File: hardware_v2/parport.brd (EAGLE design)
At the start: 65 x 56 mm, 5 parts, among them K1 PIN20X2, U1 SN74LVC161284DL

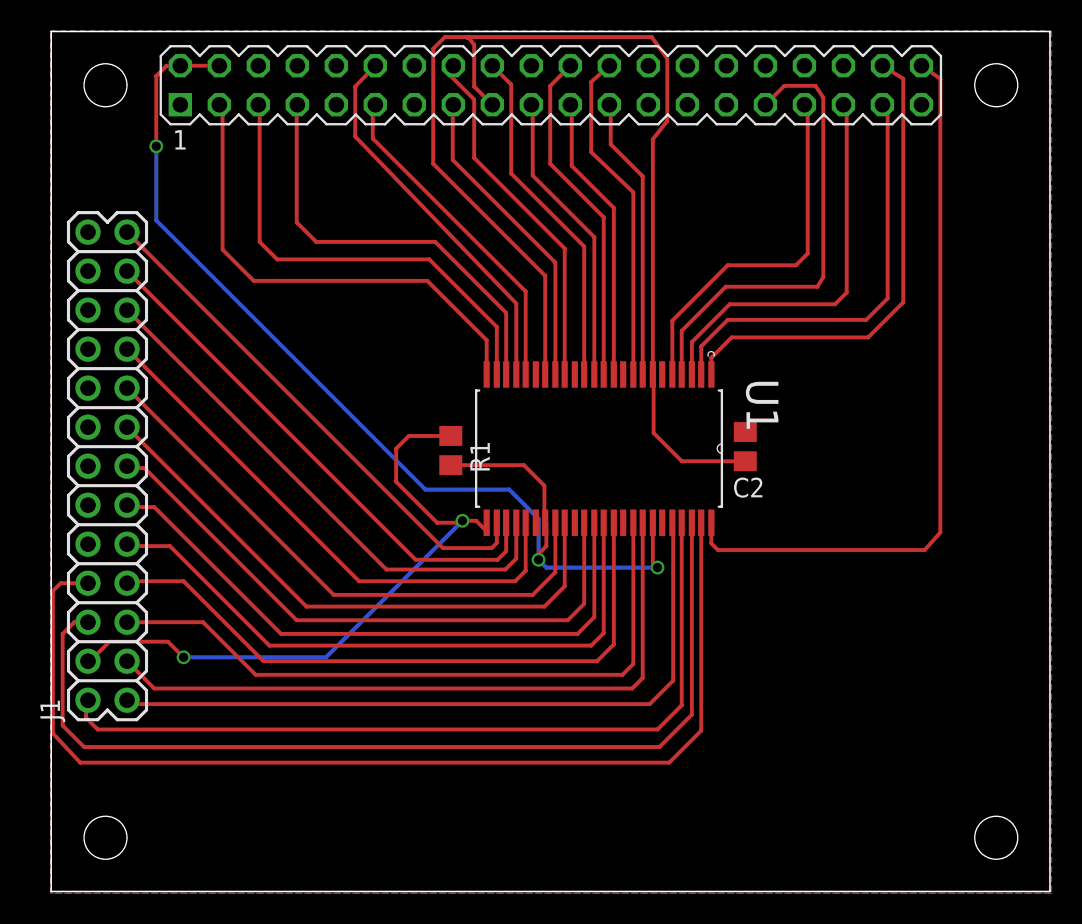
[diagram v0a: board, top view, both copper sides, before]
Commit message: hardware_v2: fix drc errors, add silk title
This version ordered from OSH Park (3 boards).
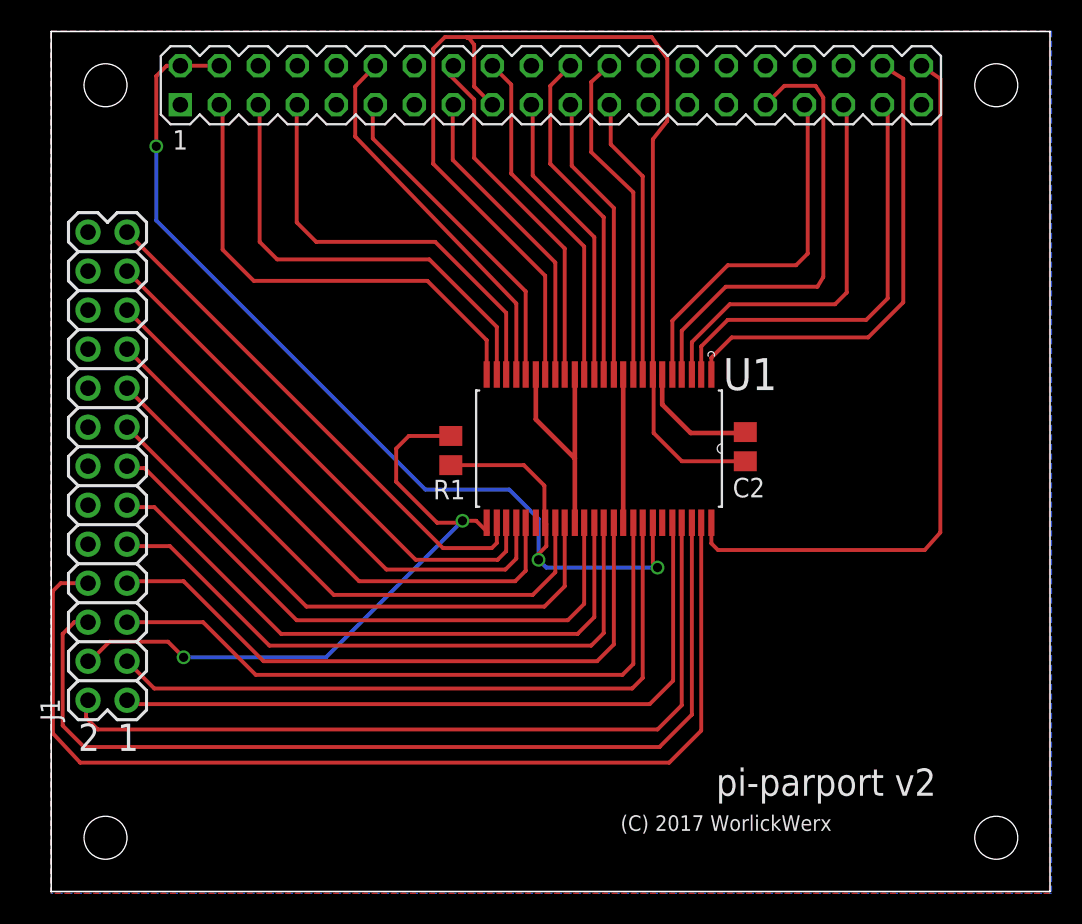
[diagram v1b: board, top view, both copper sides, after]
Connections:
- net GND: now also U1.19, U1.6
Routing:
- net GND: track 0.00 -> 34.0 mm
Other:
- board text added: "(C) 2017 WorlickWerx"
- board text added: "1"
- board text added: "2"
- board text added: "pi-parport v2"
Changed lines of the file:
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@@
 <wire x1="110.9" y1="59.8" x2="45.862" y2="59.8" width="0.1" layer="46"/>
 <circle x="49.4" y="7.3" radius="1.55" width="3.1" layer="42"/>
+<text x="50.165" y="12.954" size="1.778" layer="25">1</text>
+<text x="47.625" y="12.954" size="1.778" layer="25">2</text>
+<text x="82.931" y="7.747" size="1.016" layer="25">(C) 2017 WorlickWerx</text>
+<text x="89.154" y="10.033" size="1.778" layer="25">pi-parport v2</text>
 </plain>
 <attributes>
@@
 </element>
 <element name="J1" library="SparkFun-Connectors" package="2X13" value="" x="50.8" y="16.256" rot="R90"/>
-<element name="U1" library="worlickwerx" package="SOP63P1035X279-48N" value="SN74LVC161284DL" x="81.534" y="32.639" rot="R270">
+<element name="U1" library="worlickwerx" package="SOP63P1035X279-48N" value="SN74LVC161284DL" x="81.534" y="32.639" smashed="yes" rot="R270">
 <attribute name="SUPPLIER" value="Texas Instruments" x="81.534" y="32.639" size="1.778" layer="27" rot="R270" display="off"/>
 <attribute name="PACKAGE" value="48-SSOP" x="81.534" y="32.639" size="1.778" layer="27" rot="R270" display="off"/>
 <attribute name="MPN" value="SN74LVC161284DL" x="81.534" y="32.639" size="1.778" layer="27" rot="R270" display="off"/>
-</element>
-<element name="R1" library="resistor" package="R0805" value="1.4K" x="71.882" y="32.512" rot="R270"/>
+<attribute name="NAME" x="89.6112" y="36.449" size="2.0828" layer="25" ratio="10" rot="SR0"/>
+<attribute name="VALUE" x="70.7136" y="38.5826" size="2.0828" layer="27" ratio="10" rot="SR270"/>
+</element>
+<element name="R1" library="resistor" package="R0805" value="1.4K" x="71.882" y="32.512" smashed="yes" rot="R270">
+<attribute name="NAME" x="70.739" y="29.337" size="1.27" layer="25"/>
+<attribute name="VALUE" x="69.342" y="33.147" size="1.27" layer="27" rot="R270"/>
+</element>
 </elements>
 <signals>
@@
 <contactref element="U1" pad="39"/>
 <contactref element="U1" pad="34"/>
-<polygon width="0.254" layer="1" isolate="0.254">
+<polygon width="0.254" layer="1" isolate="0.4064">
 <vertex x="45.847" y="59.817"/>
 <vertex x="110.871" y="59.817"/>
@@
 <vertex x="45.847" y="3.683"/>
 </polygon>
-<polygon width="0.254" layer="16" isolate="0.3048">
+<polygon width="0.254" layer="16" isolate="0.4064">
 <vertex x="45.847" y="59.817"/>
 <vertex x="110.998" y="59.817"/>
@@
 <vertex x="45.847" y="3.683"/>
 </polygon>
+<wire x1="83.1088" y1="37.465" x2="83.1088" y2="27.813" width="0.3048" layer="1"/>
+<contactref element="U1" pad="19"/>
+<contactref element="U1" pad="6"/>
+<wire x1="79.9592" y1="37.465" x2="79.9592" y2="32.004" width="0.3048" layer="1"/>
+<wire x1="79.9592" y1="32.004" x2="79.9592" y2="27.813" width="0.3048" layer="1"/>
+<wire x1="85.6488" y1="37.465" x2="85.6488" y2="35.5092" width="0.3048" layer="1"/>
+<wire x1="85.6488" y1="35.5092" x2="87.503" y2="33.655" width="0.3048" layer="1"/>
+<wire x1="87.503" y1="33.655" x2="90.998" y2="33.655" width="0.3048" layer="1"/>
+<wire x1="90.998" y1="33.655" x2="91.059" y2="33.716" width="0.3048" layer="1"/>
+<wire x1="77.4192" y1="37.465" x2="77.4192" y2="34.544" width="0.3048" layer="1"/>
+<wire x1="77.4192" y1="34.544" x2="79.9592" y2="32.004" width="0.3048" layer="1"/>
+<wire x1="85.6488" y1="37.465" x2="83.1088" y2="37.465" width="0" layer="19" extent="1-1"/>
 </signal>
 <signal name="+3V3">
